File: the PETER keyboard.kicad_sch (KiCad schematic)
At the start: 146 parts, among them J1 USB_C_Receptacle_USB2.0, SW1 RotaryEncoder_Switch, SW12 RotaryEncoder_Switch, SW2 SW_Push, U1 ATmega32U4-M, Y1 Crystal_GND24_Small

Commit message: pcb, plate cleaned
stabs reversed
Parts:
- MX52: footprint MX_Only:MXOnly-2.75U-Hotswap -> MX_Only:MXOnly-2.75U-Hotswap-ReversedStabilizers
- MX53: footprint MX_Only:MXOnly-6U-Centered-Hotswap -> MX_Only:MXOnly-6U-Centered-Hotswap-ReversedStabilizers
- MX54: footprint MX_Only:MXOnly-2.25U-Hotswap -> MX_Only:MXOnly-2.25U-Hotswap-ReversedStabilizers
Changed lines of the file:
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@@
       (effects (font (size 0.508 0.508)))
     )
-    (property "Footprint" "MX_Only:MXOnly-6U-Centered-Hotswap" (id 2) (at 157.48 116.84 0)
+    (property "Footprint" "MX_Only:MXOnly-6U-Centered-Hotswap-ReversedStabilizers" (id 2) (at 157.48 116.84 0)
       (effects (font (size 1.524 1.524)) hide)
     )
@@
       (effects (font (size 0.508 0.508)))
     )
-    (property "Footprint" "MX_Only:MXOnly-2.25U-Hotswap" (id 2) (at 177.165 98.425 0)
+    (property "Footprint" "MX_Only:MXOnly-2.25U-Hotswap-ReversedStabilizers" (id 2) (at 177.165 98.425 0)
       (effects (font (size 1.524 1.524)) hide)
     )
@@
       (effects (font (size 0.508 0.508)))
     )
-    (property "Footprint" "MX_Only:MXOnly-2.75U-Hotswap" (id 2) (at 144.145 98.425 0)
+    (property "Footprint" "MX_Only:MXOnly-2.75U-Hotswap-ReversedStabilizers" (id 2) (at 144.145 98.425 0)
       (effects (font (size 1.524 1.524)) hide)
     )
@@
     )
     (path "/7d4d6e3e-91d3-472d-ba9e-24b93ec1742f"
-      (reference "MX52") (unit 1) (value "MX-NoLED") (footprint "MX_Only:MXOnly-2.75U-Hotswap")
+      (reference "MX52") (unit 1) (value "MX-NoLED") (footprint "MX_Only:MXOnly-2.75U-Hotswap-ReversedStabilizers")
     )
     (path "/0870f4c6-cf74-4d41-94d2-7eecd22517a4"
-      (reference "MX53") (unit 1) (value "MX-NoLED") (footprint "MX_Only:MXOnly-6U-Centered-Hotswap")
+      (reference "MX53") (unit 1) (value "MX-NoLED") (footprint "MX_Only:MXOnly-6U-Centered-Hotswap-ReversedStabilizers")
     )
     (path "/150cbac0-f7f3-42a2-9fee-ab866a5399d2"
-      (reference "MX54") (unit 1) (value "MX-NoLED") (footprint "MX_Only:MXOnly-2.25U-Hotswap")
+      (reference "MX54") (unit 1) (value "MX-NoLED") (footprint "MX_Only:MXOnly-2.25U-Hotswap-ReversedStabilizers")
     )
     (path "/4d37e96d-86da-49e3-9eb6-cfd76991e47b"

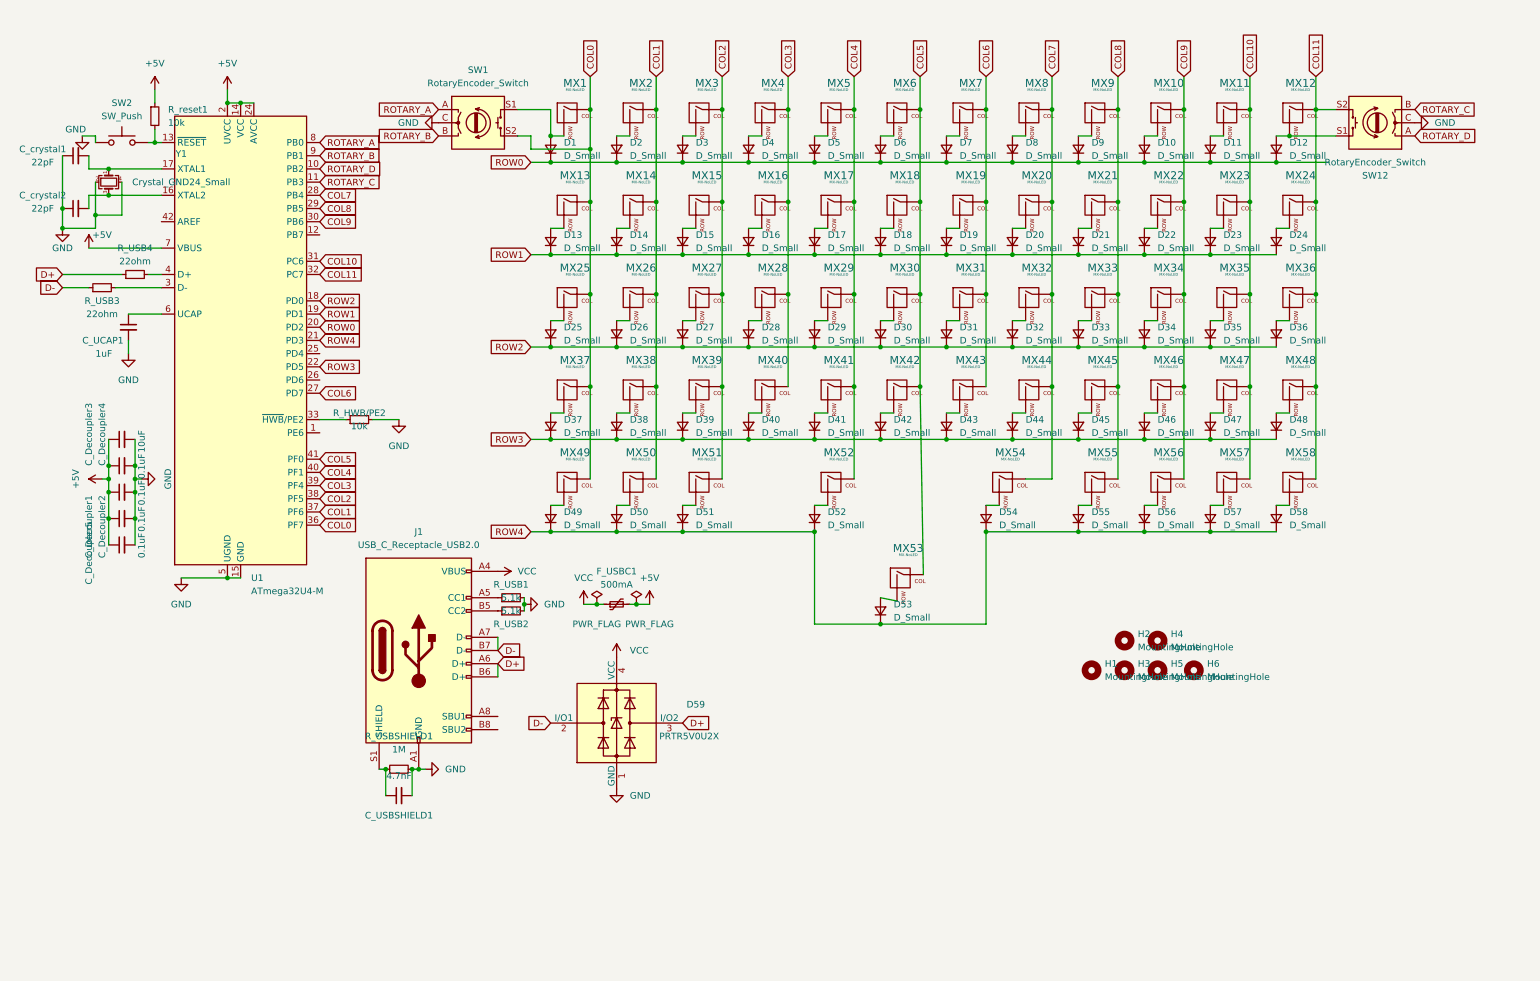
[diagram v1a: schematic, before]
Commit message: gnd fill changed, bottom mounting changed
switchplate has not been adapted, routing not working
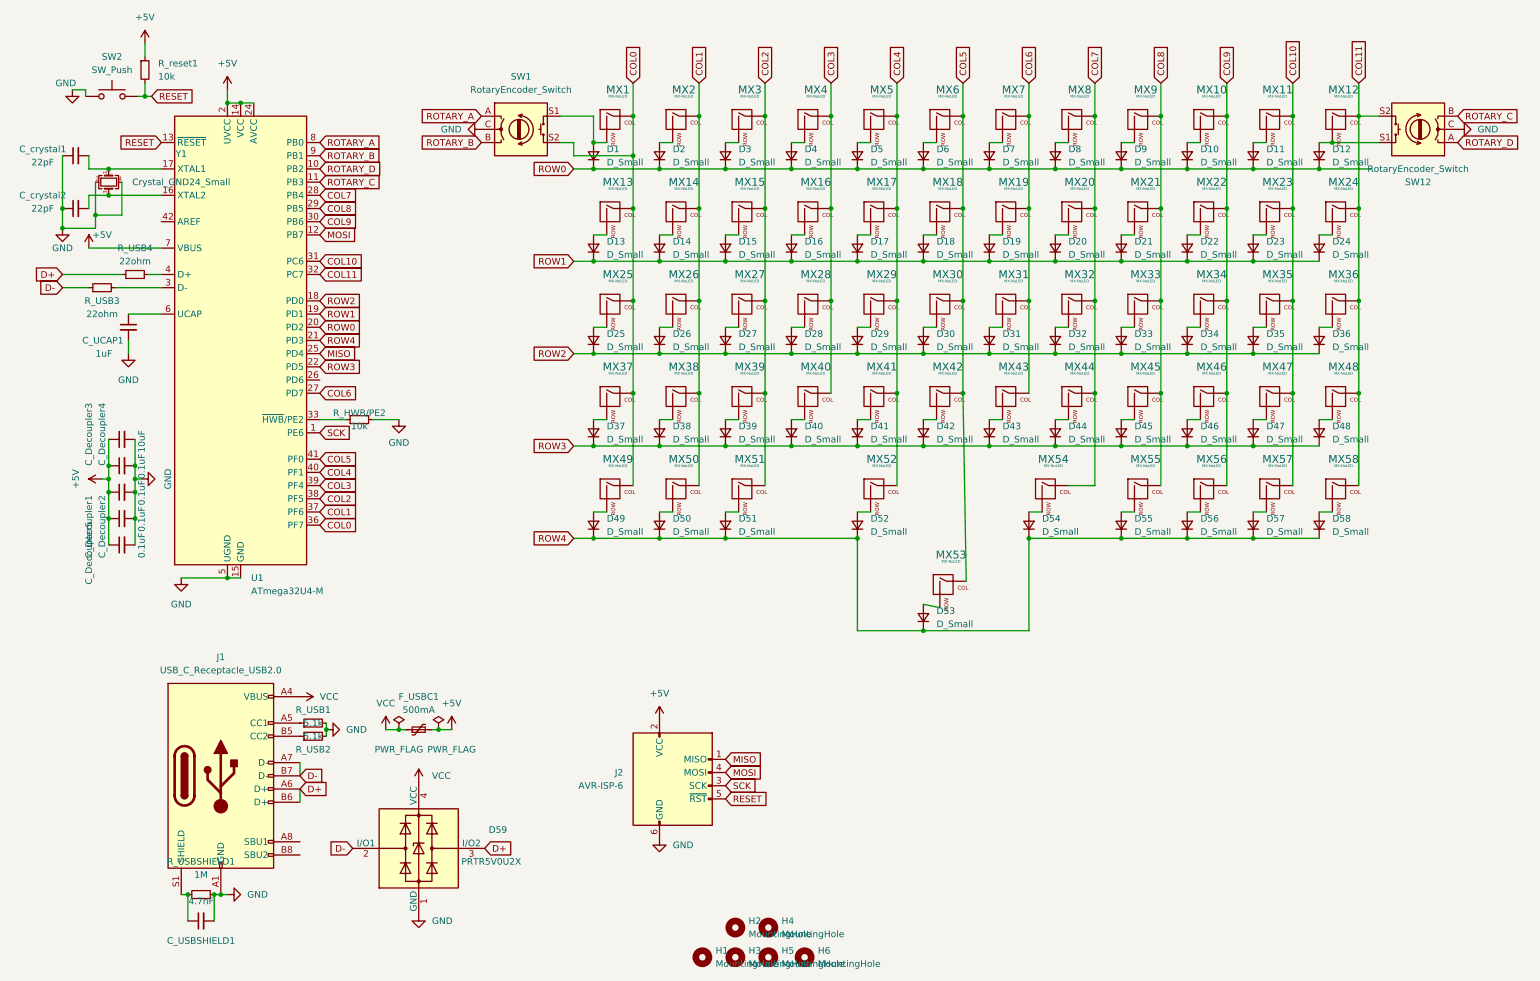
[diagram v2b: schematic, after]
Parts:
- added J2: AVR-ISP-6, random-keyboard-parts:Reset_Pretty-Mask, symbol Connector:AVR-ISP-6
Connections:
- net +5V: now also J2.2 (VCC)
- net GND: now also J2.6 (GND)
- net RESET: now reaches R_reset1.2, SW2.2, U1.13 (~{RESET})
- net RESET: now also J2.5 (~{RST})
- net SCK: now reaches U1.1 (PE6)
- net SCK: now also J2.3 (SCK)
- net MOSI: now reaches U1.12 (PB7)
- net MOSI: now also J2.4 (MOSI)
- net MISO: now reaches U1.25 (PD4)
- net MISO: now also J2.1 (MISO)
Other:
- moved on the sheet: C_USBSHIELD1, D1, D10, D11, D12, D13, D14, D15, D16, D17, D18, D19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
